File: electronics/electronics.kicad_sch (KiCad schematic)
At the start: 5 parts, among them U1 ESP32-C6-WROOM-1

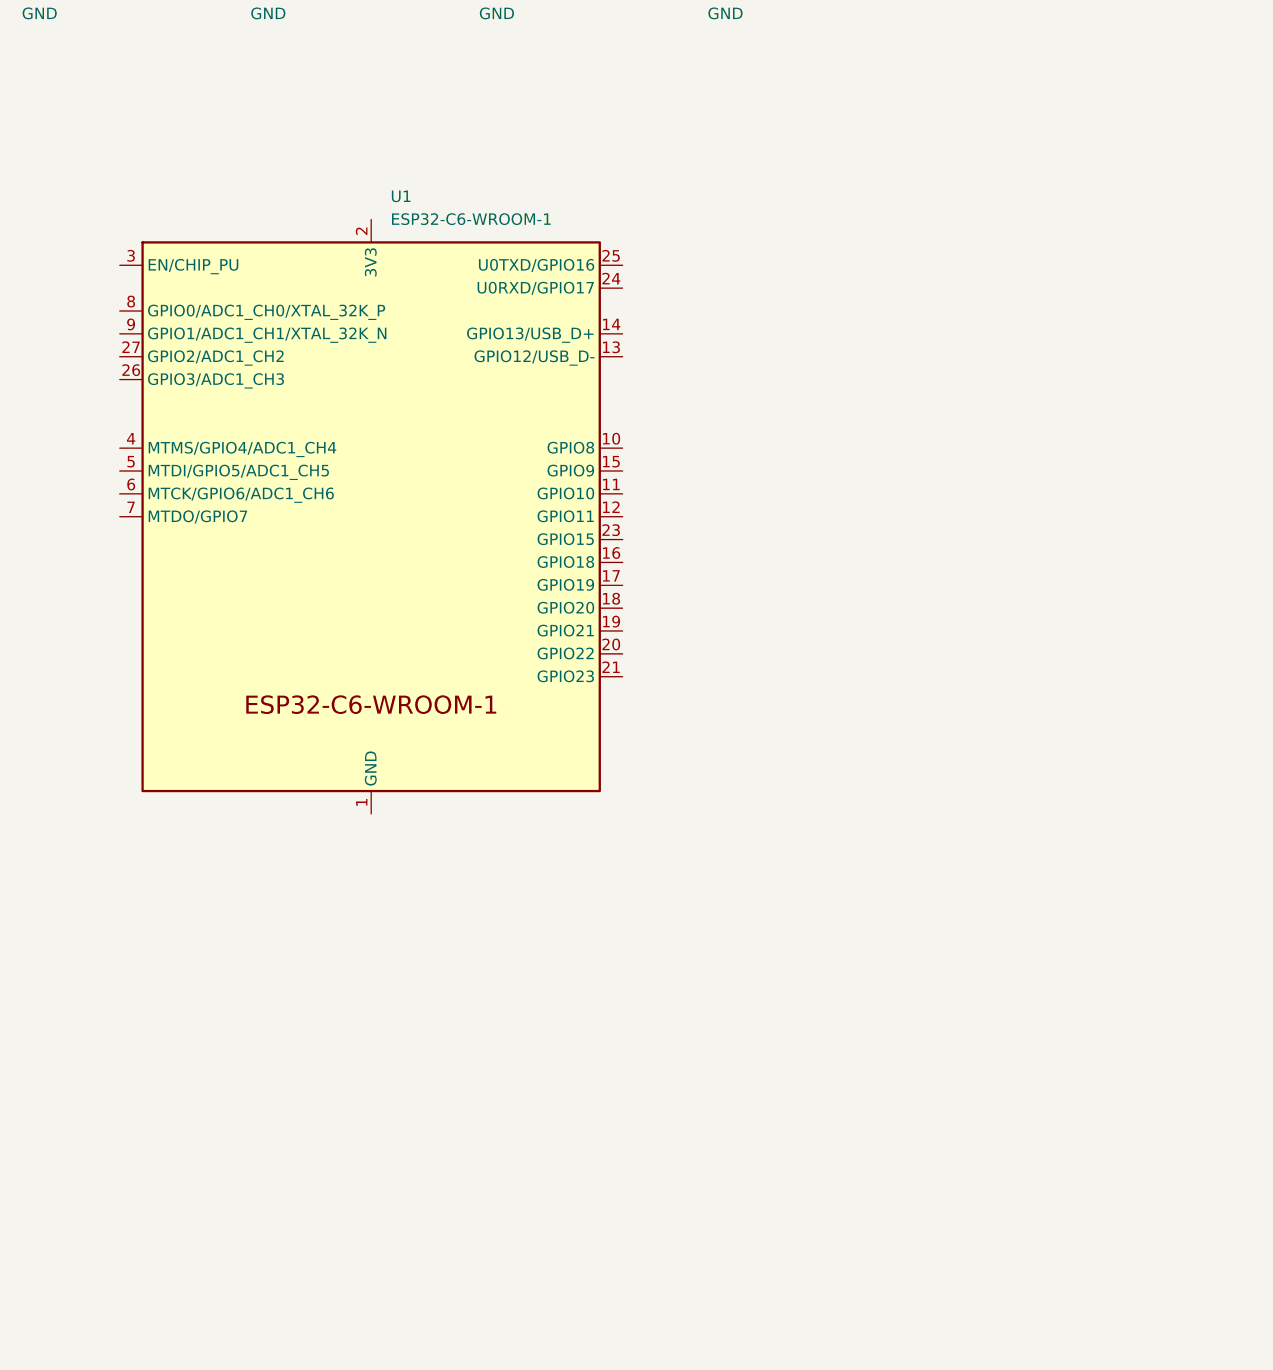
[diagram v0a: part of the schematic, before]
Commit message: pcb: add mcu, power regulator and usb-c connector
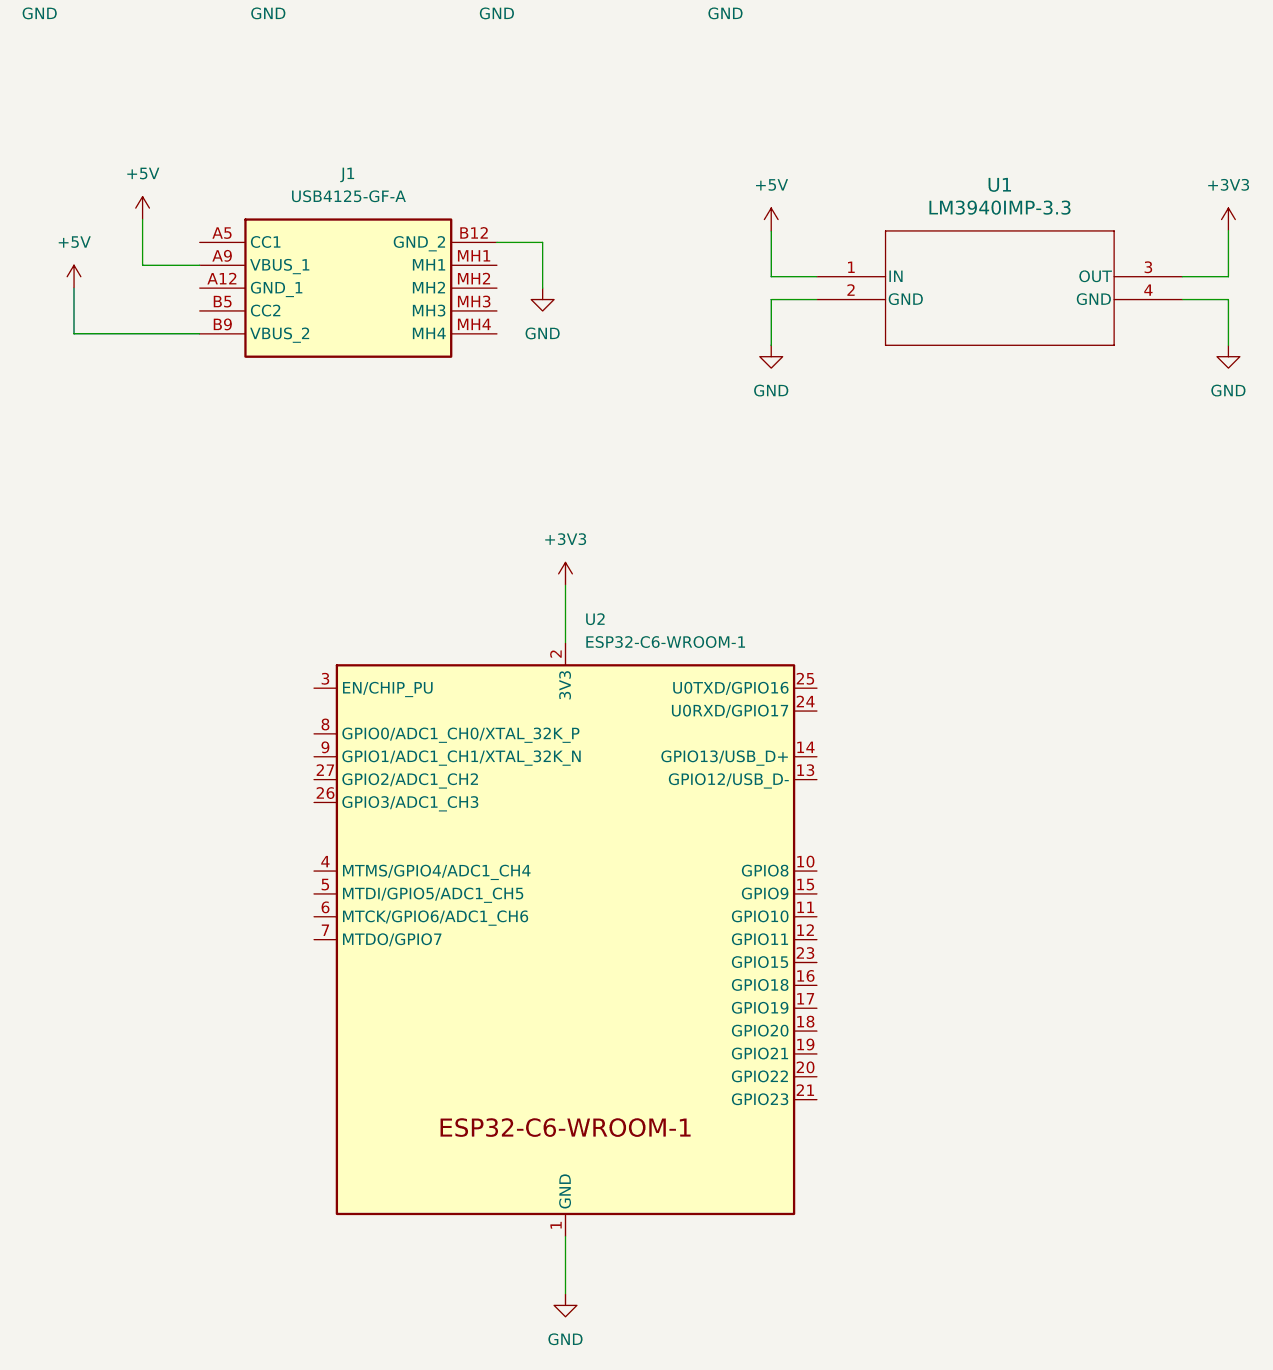
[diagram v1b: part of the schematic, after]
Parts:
- removed U1: ESP32-C6-WROOM-1, PCM_Espressif:ESP32-C6-WROOM-1, symbol PCM_Espressif:ESP32-C6-WROOM-1
- added J1: USB4125-GF-A, USB4125GFA, symbol USB4125-GF-A:USB4125-GF-A
- added U1: LM3940IMP-3.3, footprints:MP04A, symbol Symbols:LM3940IMP-3.3
- added U2: ESP32-C6-WROOM-1, PCM_Espressif:ESP32-C6-WROOM-1, symbol PCM_Espressif:ESP32-C6-WROOM-1
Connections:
- net GND: now also J1.B12 (GND_2), U1.2 (GND), U1.4 (GND), U2.1 (GND), U2.28 (GND), U2.29 (GND)
- new net +3V3: U1.3 (OUT), U2.2 (3V3)
- new net +5V: J1.A9 (VBUS_1), J1.B9 (VBUS_2), U1.1 (IN)

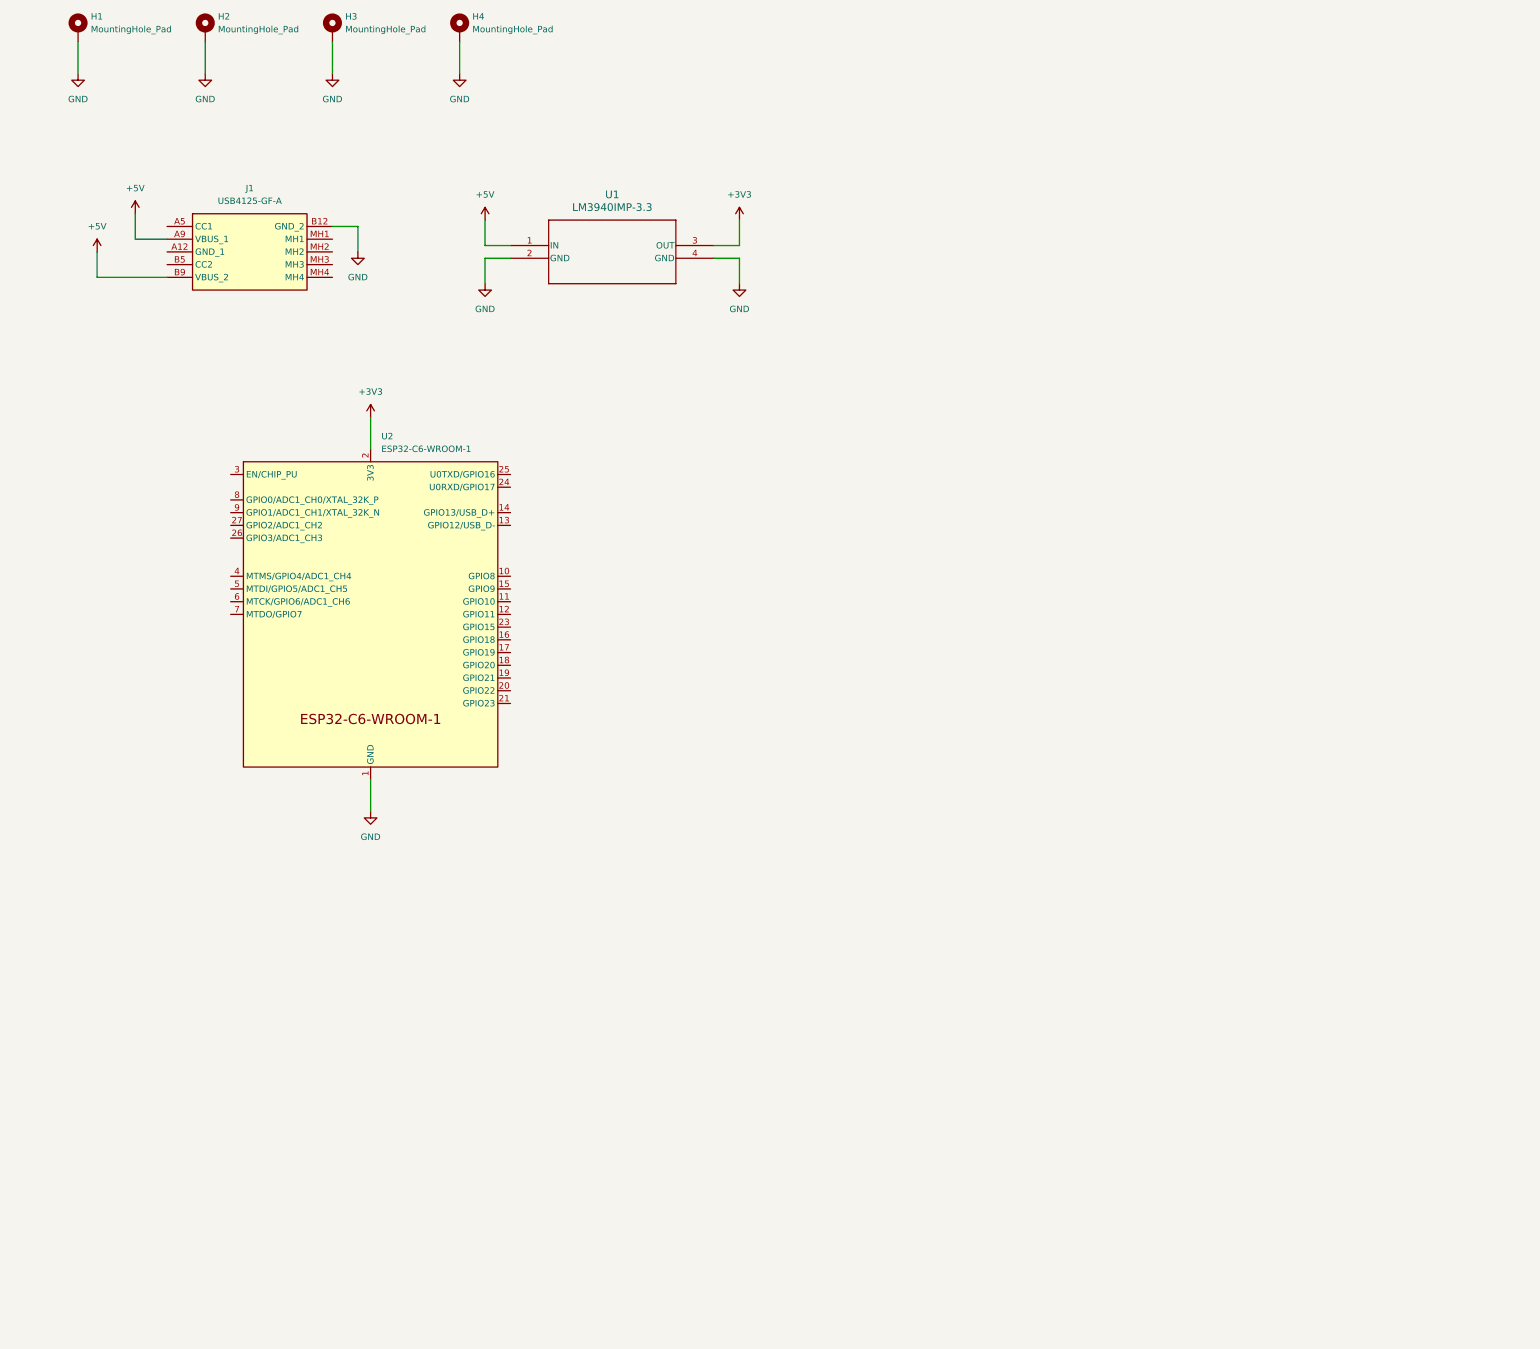
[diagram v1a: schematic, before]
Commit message: pcb: add usb power and data connections
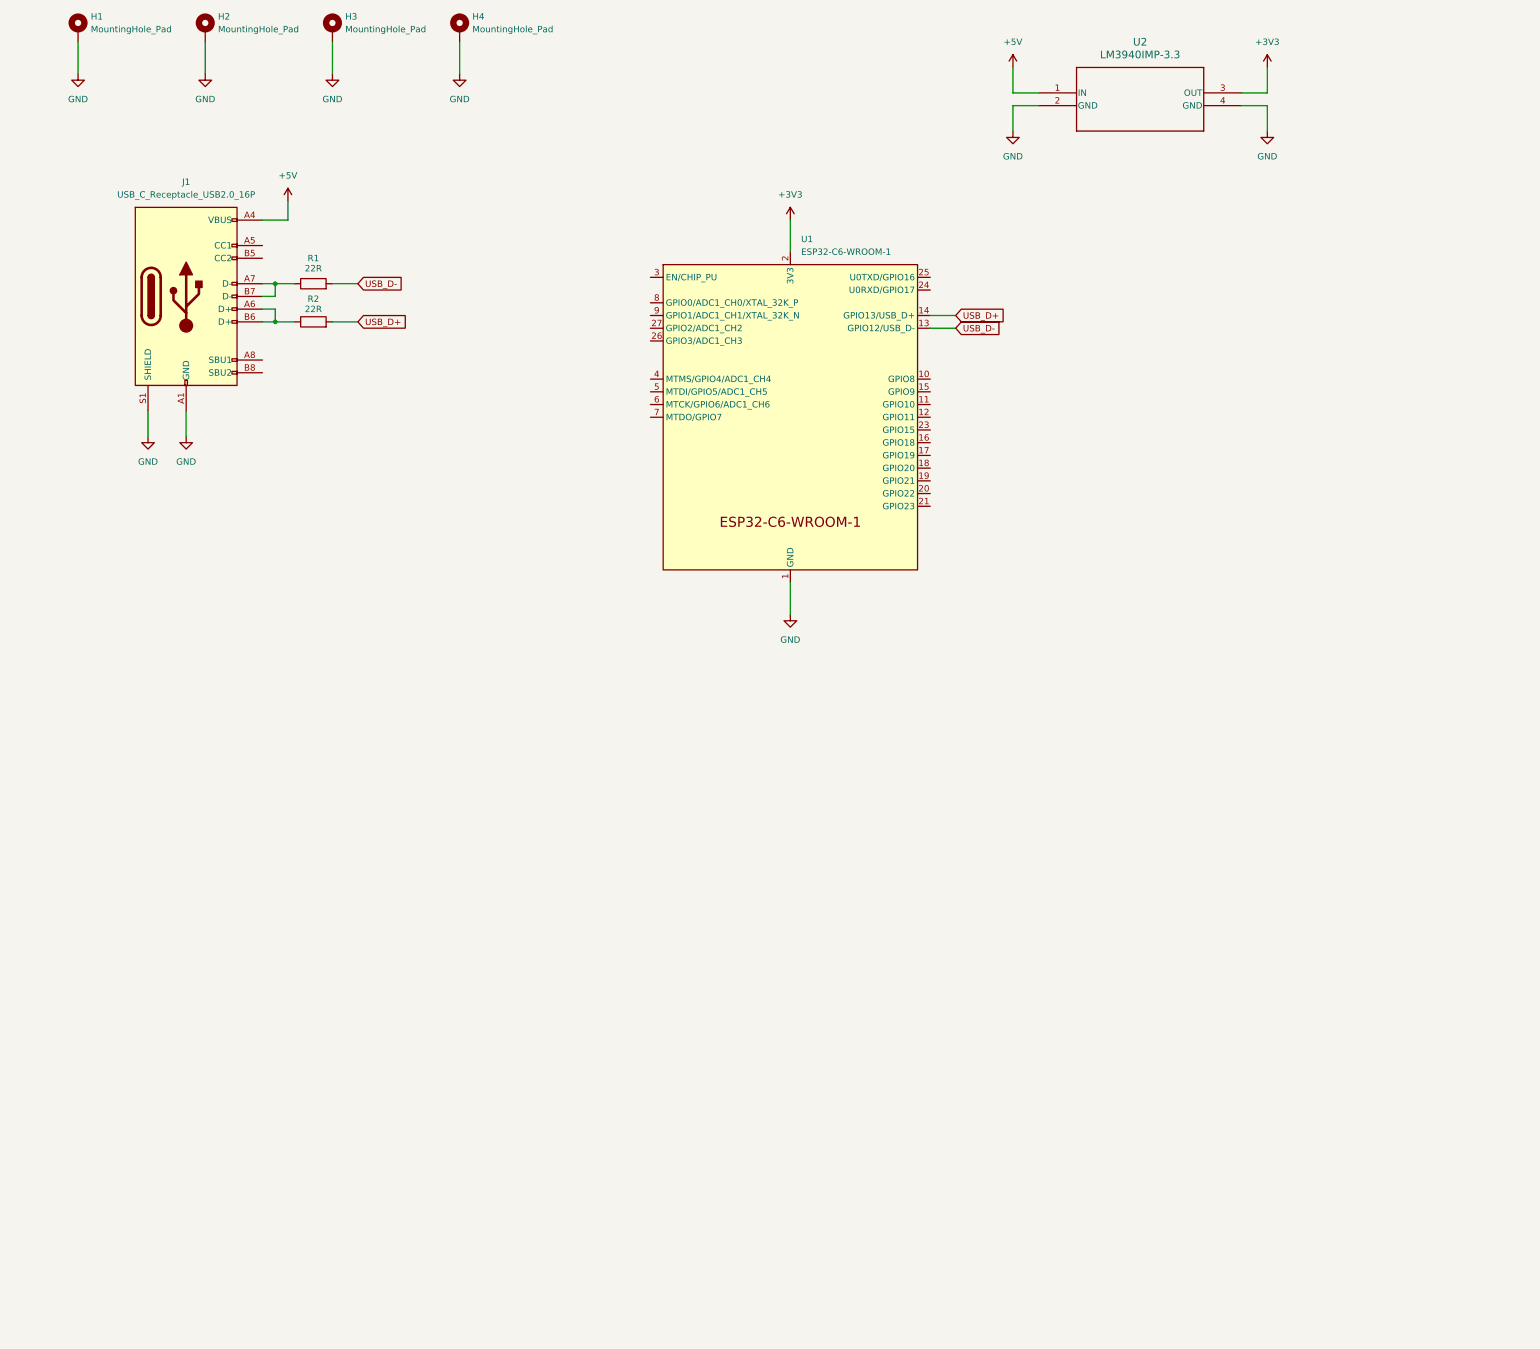
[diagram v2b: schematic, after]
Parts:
- removed J1: USB4125-GF-A, USB4125GFA, symbol USB4125-GF-A:USB4125-GF-A
- added J1: USB_C_Receptacle_USB2.0_16P, Connector_USB:USB_C_Receptacle_GCT_USB4105-xx-A_16P_TopMnt_Horizontal, symbol Connector:USB_C_Receptacle_USB2.0_16P
- added R1, R2: 22R, Resistor_SMD:R_0805_2012Metric_Pad1.20x1.40mm_HandSolder, symbol Device:R
- renumbered U2 to U1, U1 to U2
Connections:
- net +5V: now also J1.A4 (VBUS), J1.A9 (VBUS), J1.B4 (VBUS), J1.B9 (VBUS)
- net GND: now also J1.A1 (GND), J1.A12 (GND), J1.B1 (GND), J1.B12 (GND), J1.S1 (SHIELD)
- net USB_D-: now reaches U1.13 (GPIO12/USB_D-)
- net USB_D-: now also R1.2
- net USB_D+: now reaches U1.14 (GPIO13/USB_D+)
- net USB_D+: now also R2.2
- new net: J1.A7 (D-), J1.B7 (D-), R1.1
- new net: J1.A6 (D+), J1.B6 (D+), R2.1
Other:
- moved on the sheet: U1, U2

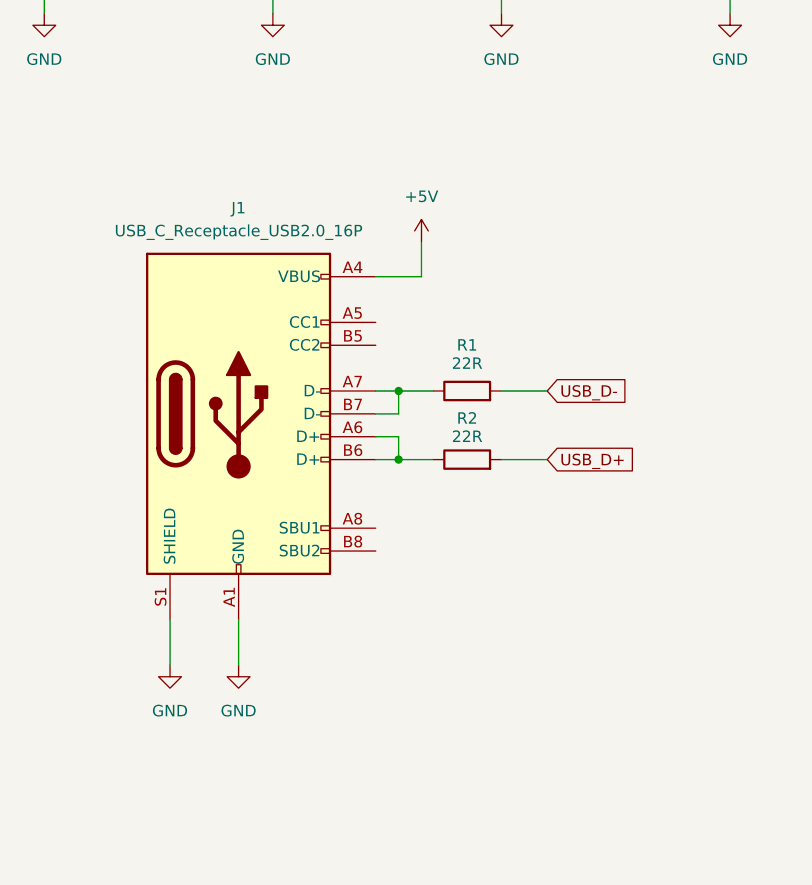
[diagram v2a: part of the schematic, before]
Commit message: pcb: add 5.1k pull-downs to usb cc1/cc2
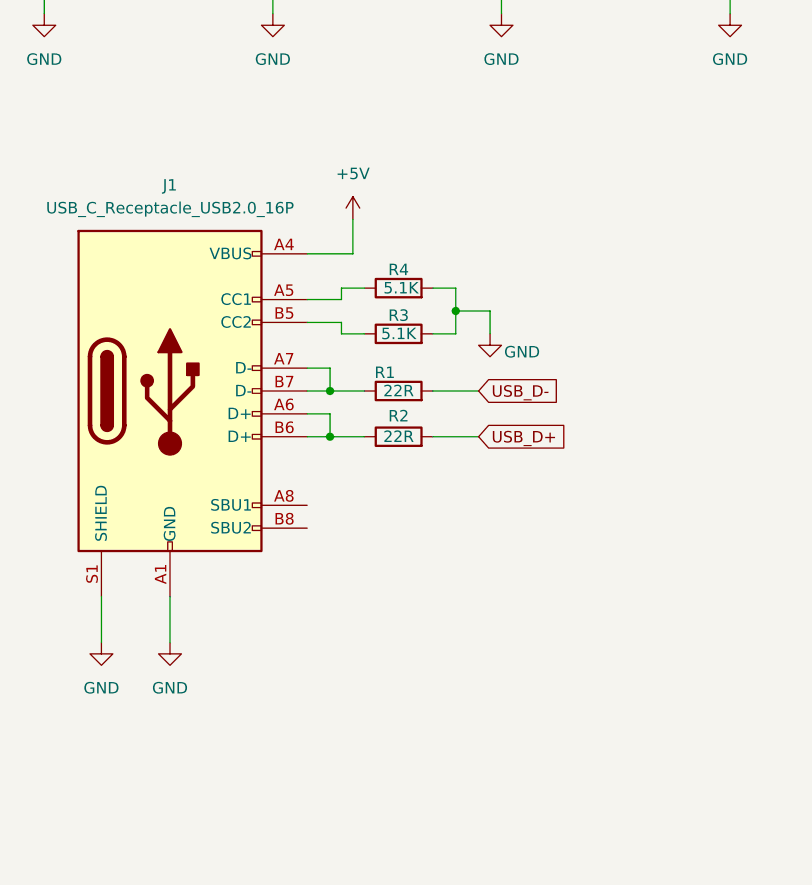
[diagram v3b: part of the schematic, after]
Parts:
- added R3, R4: 5.1K, Resistor_SMD:R_0805_2012Metric_Pad1.20x1.40mm_HandSolder, symbol Device:R
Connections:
- net GND: now also R3.2, R4.2
- net at J1.A5 (CC1): now also R4.1
- net at J1.B5 (CC2): now also R3.1
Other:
- moved on the sheet: J1, R1, R2

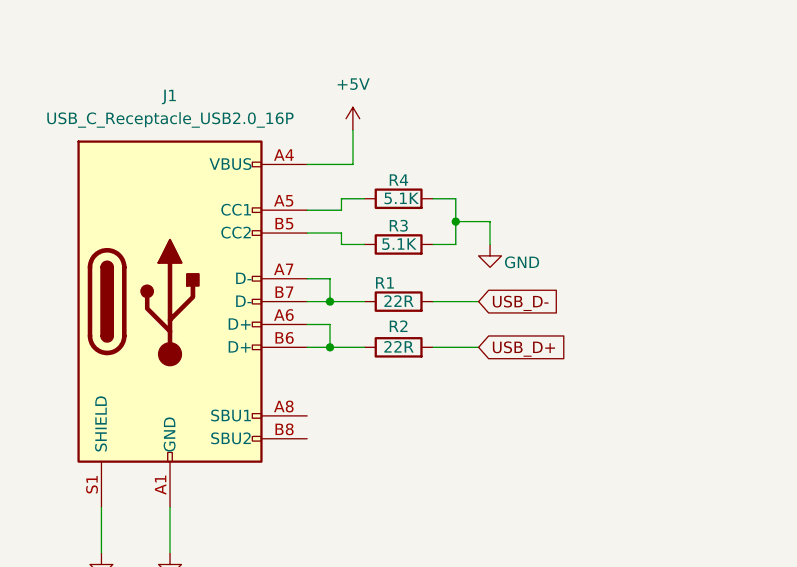
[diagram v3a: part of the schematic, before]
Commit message: pcb: add 5.1k pull-downs to usb cc1/cc2 to pcb
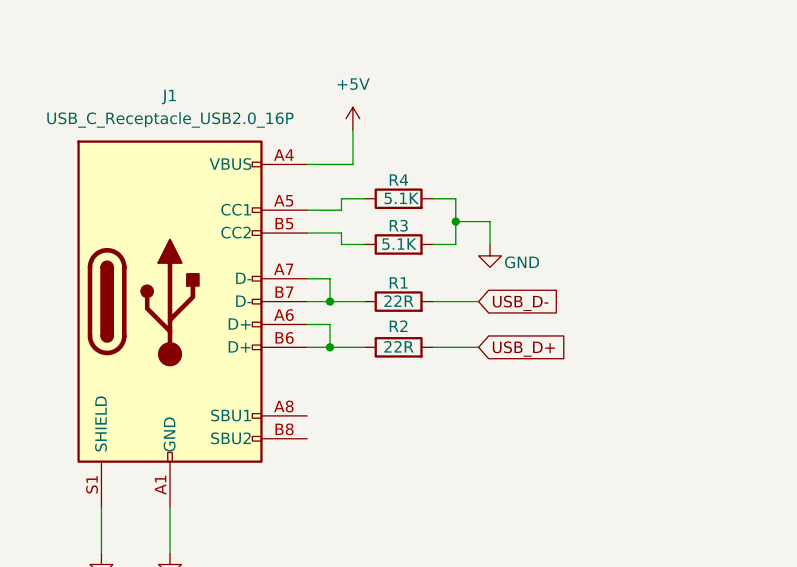
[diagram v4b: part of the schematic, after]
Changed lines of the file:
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@@
 		(dnp no)
 		(property "Reference" "R1"
-			(at 63.246 71.628 90)
+			(at 64.77 71.628 90)
 			(effects
 				(font
